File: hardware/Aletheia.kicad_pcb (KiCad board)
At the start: 12 copper layers, 94 x 127 mm, 85 parts, among them J101 Conn_01x04, J201 4090 USB-C, J202 9V battery, SW101 SW_DIP_x08, SW102 SW_DIP_x08, SW104 SW_DIP_x04, SW105 G19AP, SW301 Q/1/STOP, SW302 W/2/CH0, SW303 E/3/CH1, SW304 R/4/CH2, SW305 T/5/CH3, SW306 Y/6/_, SW307 U/7/-, SW308 I/8/+, SW309 O/9/=, SW310 P/0, SW311 A/!/`, SW312 S/"/CH4, SW313 D/$/CH5, SW314 F/%/CH6, SW315 G/^/CH7, SW316 H/&/{, SW317 J/*/}, SW318 K/(/[, SW319 L/)/], SW320 BKSP/DEL, SW321 SHIFT, SW322 Z/\/|, SW323 X/;/:, SW324 C/'/@, SW325 V/#/~, SW326 B/,/<, SW327 N/./>, SW328 M///?, SW329 SYM, SW330 SPC/ENT, U101 W65C02S6TPG-14, U102 AS6C1008-55PCN, U103 W65C22N6TPG-14, U104 74LS04, U105 74LS08, U106 74LS21, U201 LP2954AIT/NOPB, U301 MCP23S17_SP, U302 NHD-0420DZ-NSW-BBW, Y101 ECS-100AX-010

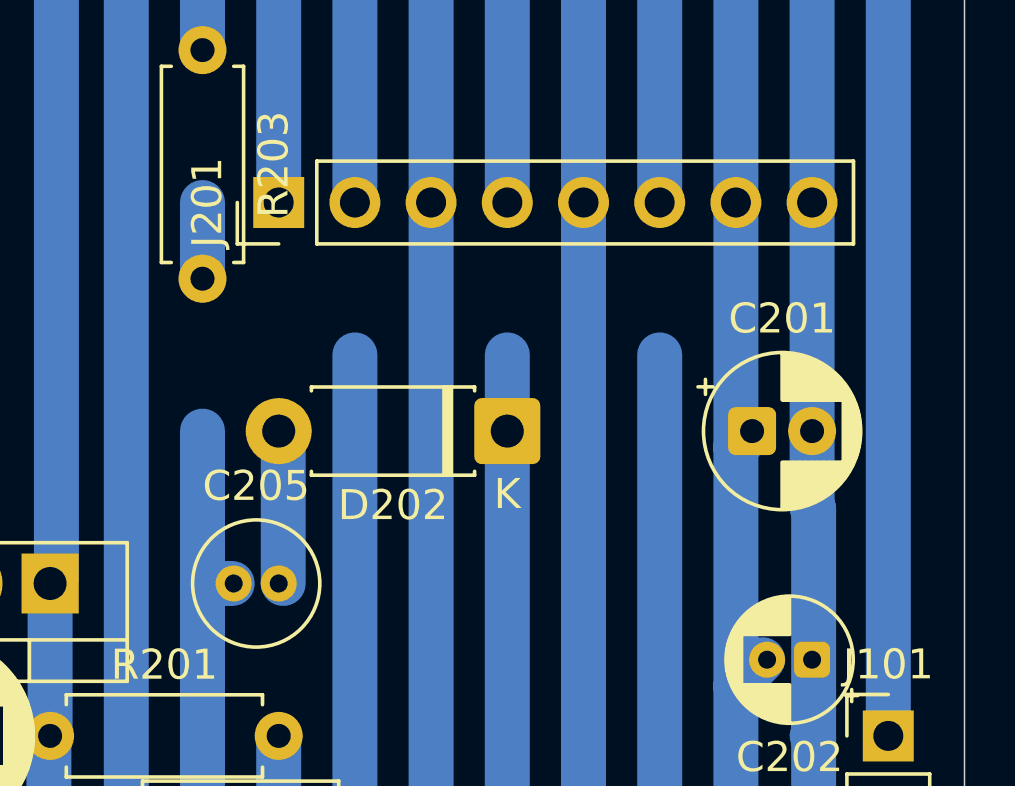
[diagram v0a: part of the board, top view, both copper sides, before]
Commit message: Add in missing ground wire on hardware
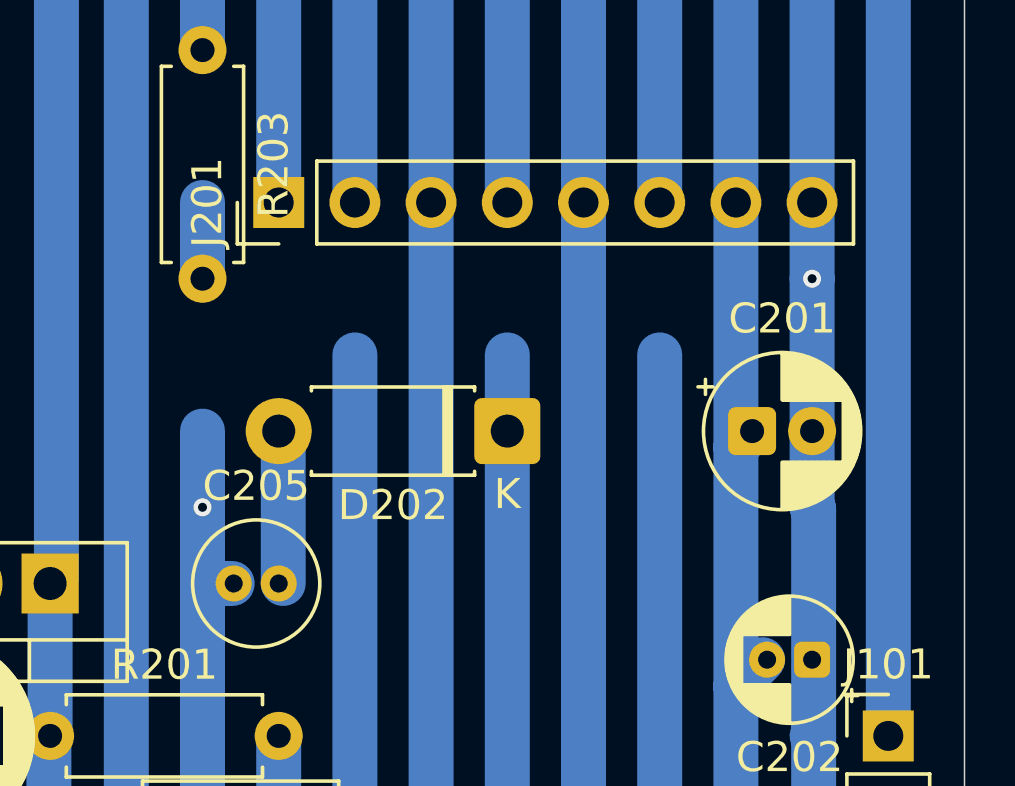
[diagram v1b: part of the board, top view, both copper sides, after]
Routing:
- net GND: track 820.1 -> 845.0 mm, vias 5 -> 7
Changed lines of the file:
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@@
+	)
+	(via
+		(at 119.38 48.26)
+		(size 0.6)
+		(drill 0.3)
+		(layers "F.Cu" "B.Cu")
+		(net 1)
 	)
 	(via
@@
 	)
 	(via
+		(at 139.7 40.64)
+		(size 0.6)
+		(drill 0.3)
+		(layers "F.Cu" "B.Cu")
+		(net 1)
+	)
+	(via
 		(at 106.629 60.96)
 		(size 0.6)
@@
 	(segment
 		(start 139.7 38.1)
-		(end 139.7 45.72)
+		(end 139.7 40.64)
 		(width 1.5)
 		(layer "B.Cu")
@@
 	)
 	(segment
+		(start 139.7 40.64)
+		(end 139.7 45.72)
+		(width 1.5)
+		(layer "B.Cu")
+		(net 1)
+	)
+	(segment
 		(start 116.84 58.756)
 		(end 116.84 27.94)
@@
 	(segment
 		(start 119.38 50.8)
-		(end 119.38 45.72)
+		(end 119.38 48.26)
 		(width 1.5)
 		(layer "B.Cu")
@@
 		(start 139.7 104.14)
 		(end 139.7 99.06)
+		(width 1.5)
+		(layer "B.Cu")
+		(net 1)
+	)
+	(segment
+		(start 119.38 48.26)
+		(end 119.38 45.72)
 		(width 1.5)
 		(layer "B.Cu")
@@
 	)
 	(segment
+		(start 119.38 45.72)
+		(end 119.38 48.26)
+		(width 0.2)
+		(layer "In3.Cu")
+		(net 1)
+	)
+	(segment
 		(start 93.98 101.6)
 		(end 117.88 101.6)
@@
 		(width 0.2)
 		(layer "In3.Cu")
+		(net 1)
+	)
+	(segment
+		(start 124.46 40.64)
+		(end 119.38 45.72)
+		(width 0.2)
+		(layer "In3.Cu")
+		(net 1)
+	)
+	(segment
+		(start 139.7 40.64)
+		(end 124.46 40.64)
+		(width 0.2)
+		(layer "In3.Cu")
